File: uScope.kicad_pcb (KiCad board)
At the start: 2 copper layers, 315 x 100 mm, 626 parts, among them J1 Pump+, J10 Nucleo_SWD, J11 STLinkV2, J12 Nucleo_SWD, J13 Conn_02x10_Odd_Even, J14 Conn_02x10_Odd_Even, J15 Conn_02x03_Odd_Even, J16 Conn_02x03_Odd_Even, J2 Pump-, J3 U_E, J4 U_F, J5 Conn_01x02, J6 U_K, J7 Anode, J8 USB_B_Micro, J9 STLinkV2, Q10 BC817, Q11 BC807, Q12 BSS138, Q13 BSS138, Q14 BSS138, Q15 BSS138, Q16 BSS138, Q17 BSS138, Q18 BSS138, Q19 BSS138, Q20 BSS138, Q21 BC817, Q3 BC817, Q4 BC807, Q5 BUK98150-55A, Q6 BUK98150-55A, Q7 BUK98150-55A, Q8 BUK98150-55A, Q9 BSS84, SW10 ESC, SW11 RST, SW2 set_current, SW3 PWRON, SW4 RST, SW5 Encoder, SW7 UP, SW8 DOWN, SW9 ENTER, U1 K, U11 LMC6482, U12 LMC6482, U13 LM321, U14 DAC8564, U15 LM321, U16 LM321, U17 LM321, U18 LM317L_SOT89, U19 PAM242x, U2 E, U20 LM337L_SO8, U21 TPS613222ADBV, U22 LP2985-3.3, U23 BQ24079RGT, U24 Holder 2x18650, U25 LCD_I2C, U26 STM32L431RBTx, U27 ADS131M06, U28 OPTI128, U29 QSE159, U3 F, U30 SN74LVC1G14DRL, U31 QSE159, U32 SN74LVC1G14DRL, U33 ADS131M06, U34 STM32L431RBTx, U35 LM317L_SOT89, U36 LP2985-3.3, U37 TL432, U38 TC7660S, U39 LM337L_SO8, U4 Pump, U5 INA128, U6 RHV2-1212S/R20, U8 LMC6482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

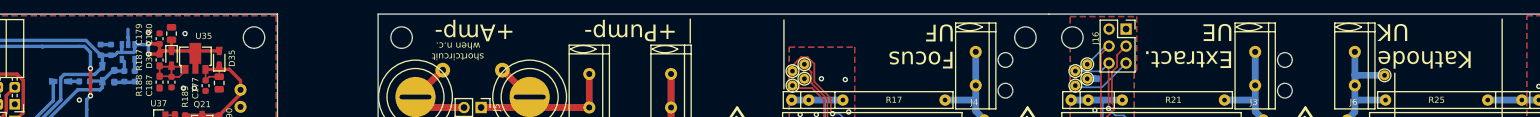
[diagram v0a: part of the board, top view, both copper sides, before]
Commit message: - as-built changes - add custom library elements
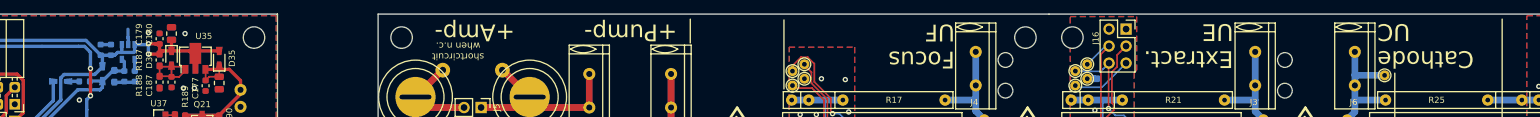
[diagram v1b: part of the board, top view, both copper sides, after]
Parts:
- removed the REF** at (268.2, 33.1) (x2)
- removed the REF** at (226.8, 33.1) (x2)
- removed the REF** at (78.6, 50.5) (x2)
- added REF**: Symbol_HighVoltage_Type2_CopperTop_VerySmall, Symbol:Symbol_HighVoltage_Type2_CopperTop_VerySmall, F.Cu at (268.2, 33.1)
- added REF**: Symbol_HighVoltage_Type2_CopperTop_VerySmall, Symbol:Symbol_HighVoltage_Type2_CopperTop_VerySmall, B.Cu at (268.2, 33.1)
- added REF**: Symbol_HighVoltage_Type2_CopperTop_VerySmall, Symbol:Symbol_HighVoltage_Type2_CopperTop_VerySmall, F.Cu at (226.8, 33.1)
- added REF**: Symbol_HighVoltage_Type2_CopperTop_VerySmall, Symbol:Symbol_HighVoltage_Type2_CopperTop_VerySmall, B.Cu at (226.8, 33.1)
- added REF**: Symbol_Highvoltage_Type2_CopperTop_Small, Symbol:Symbol_Highvoltage_Type2_CopperTop_Small, B.Cu at (78.6, 50.5)
- added REF**: Symbol_Highvoltage_Type2_CopperTop_Small, Symbol:Symbol_Highvoltage_Type2_CopperTop_Small, F.Cu at (78.6, 50.5)
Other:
- board text added: "Cathode UC"
- board text removed: "Kathode UK"
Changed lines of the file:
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@@
     (thickness 1.6)
     (drawings 94)
-    (tracks 3745)
+    (tracks 3744)
     (zones 0)
     (modules 626)
@@
     (35 F.Paste user)
     (36 B.SilkS user hide)
-    (37 F.SilkS user hide)
+    (37 F.SilkS user)
     (38 B.Mask user)
     (39 F.Mask user)
@@
   )
   (setup
-    (last_trace_width 0.5)
+    (last_trace_width 0.25)
     (user_trace_width 0.1778)
     (user_trace_width 0.5)
@@
     (effects (font (size 2.5 2.5) (thickness 0.4)) (justify left))
   )
-  (gr_text "Kathode\nUK" (at 278.9555 19.685 180) (layer F.SilkS)
+  (gr_text "Cathode\nUC" (at 278.9555 19.685 180) (layer F.SilkS)
     (effects (font (size 2.5 2.5) (thickness 0.4)) (justify right))
   )
@@
   (segment (start 89.57261 30.604797) (end 86.56761 30.604797) (width 0.5) (layer B.Cu) (net 142))
   (segment (start 86.56761 30.604797) (end 83.26561 30.604797) (width 0.5) (layer B.Cu) (net 142))
-  (segment (start 79.883 19.812) (end 80.01 19.939) (width 0.5) (layer B.Cu) (net 142))
   (via (at 87.122 27.178) (size 0.8) (drill 0.4) (layers F.Cu B.Cu) (net 142))
   (segment (start 86.56761 29.25639) (end 86.56761 30.604797) (width 0.5) (layer B.Cu) (net 142))
